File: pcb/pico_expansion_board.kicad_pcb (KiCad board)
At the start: 4 copper layers, 99.1 x 69.8 mm, 53 parts, among them IC1 TPS5450DDA, J1 DC12V/24V, J10 CAN_L, J2 TMC2209 Motor 1, J3 TMC2209 Motor 2, J4 Motor 1, J5 Motor 2, J6 Straight Through, J7 NULL Modem, J8 EXP1, J9 EXP2, SW1 SW_Push, U1 MAX232, U2 MCP2542FDxMF, U3 Pico, U5 CAT24C256

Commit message: Update to v3
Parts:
- removed the C2 at (98.6, 78.5)
- removed the C3 at (94.2, 85.9)
- removed J10: CAN_L, TerminalBlock:TerminalBlock_bornier-2_P5.08mm
- removed J7: NULL Modem, Connector_Dsub:DSUB-9_Male_Horizontal_P2.77x2.84mm_EdgePinOffset7.70mm_Housed_MountingHolesOffset9.12mm
- removed JP9: 120JP, Connector_PinHeader_2.00mm:PinHeader_1x02_P2.00mm_Vertical
- removed the R1 at (111.3, 72.1)
- removed the TP5 at (89.2, 102.9)
- removed the U2 at (94.2, 80.5)
- added C14: 0.1uF, Capacitor_SMD:C_0805_2012Metric_Pad1.18x1.45mm_HandSolder, F.Cu at (94.9, 49.1)
- added C15: 10nF, Capacitor_SMD:C_0805_2012Metric_Pad1.18x1.45mm_HandSolder, F.Cu at (33.0, 106.7)
- added C16: 10nF, Capacitor_SMD:C_0805_2012Metric_Pad1.18x1.45mm_HandSolder, F.Cu at (33.0, 109.7)
- added D2: GREEN, Diode_SMD:D_0805_2012Metric_Pad1.15x1.40mm_HandSolder, F.Cu at (24.0, 106.7)
- added D3: RED, Diode_SMD:D_0805_2012Metric_Pad1.15x1.40mm_HandSolder, F.Cu at (24.0, 109.7)
- added D4: RED, Diode_SMD:D_0805_2012Metric_Pad1.15x1.40mm_HandSolder, F.Cu at (24.0, 112.7)
- added JP5: ~, Connector_PinSocket_2.00mm:PinSocket_1x03_P2.00mm_Vertical, F.Cu at (39.1, 81.9)
- added JP6: ~, Connector_PinSocket_2.00mm:PinSocket_1x03_P2.00mm_Vertical, F.Cu at (43.2, 81.9)
- added JP7: ~, Connector_PinSocket_2.00mm:PinSocket_1x03_P2.00mm_Vertical, F.Cu at (47.2, 81.9)
- added R3: 10K, Resistor_SMD:R_0805_2012Metric_Pad1.20x1.40mm_HandSolder, F.Cu at (88.1, 92.5)
- added R5: 10K, Resistor_SMD:R_0805_2012Metric_Pad1.20x1.40mm_HandSolder, F.Cu at (88.1, 96.8)
- added R6: 4.7k, Resistor_SMD:R_0805_2012Metric_Pad1.20x1.40mm_HandSolder, F.Cu at (94.9, 52.1)
- added R7: 300, Resistor_SMD:R_0805_2012Metric_Pad1.20x1.40mm_HandSolder, F.Cu at (28.6, 106.6)
- added R8: 680, Resistor_SMD:R_0805_2012Metric_Pad1.20x1.40mm_HandSolder, F.Cu at (28.6, 109.6)
- added R9: 4.7k, Resistor_SMD:R_0805_2012Metric_Pad1.20x1.40mm_HandSolder, F.Cu at (28.6, 112.5)
- added U4: 74LVC1G125, Package_TO_SOT_SMD:SOT-353_SC-70-5_Handsoldering, F.Cu at (100.3, 50.5)
- added U5: AMS1117-3.3, Package_TO_SOT_SMD:SOT-223-3_TabPin2, F.Cu at (26.5, 101.0)
- C1: renamed from C5; footprint Capacitor_SMD:C_0805_2012Metric -> Capacitor_SMD:C_0805_2012Metric_Pad1.18x1.45mm_HandSolder
- C10: renamed from C17; footprint Capacitor_SMD:C_0805_2012Metric -> Capacitor_SMD:C_0805_2012Metric_Pad1.18x1.45mm_HandSolder
- C11: renamed from C8; value 10uF -> 0.1uF; footprint Capacitor_SMD:C_0805_2012Metric -> Capacitor_SMD:C_0805_2012Metric_Pad1.18x1.45mm_HandSolder
- C13: renamed from C19; footprint Capacitor_SMD:C_0805_2012Metric -> Capacitor_SMD:C_0805_2012Metric_Pad1.18x1.45mm_HandSolder
- C2: renamed from C1; value 1uF -> 0.1uF; footprint Capacitor_SMD:C_0805_2012Metric -> Capacitor_SMD:C_0805_2012Metric_Pad1.18x1.45mm_HandSolder
- C3: renamed from C9; footprint Capacitor_SMD:C_0805_2012Metric -> Capacitor_SMD:C_0805_2012Metric_Pad1.18x1.45mm_HandSolder
- C4: renamed from C16; footprint Capacitor_SMD:C_0805_2012Metric -> Capacitor_SMD:C_0805_2012Metric_Pad1.18x1.45mm_HandSolder
- C5: renamed from C4; value 1uF -> 0.1uF; footprint Capacitor_SMD:C_0805_2012Metric -> Capacitor_SMD:C_0805_2012Metric_Pad1.18x1.45mm_HandSolder
- C6: value 1uF -> 0.1uF; footprint Capacitor_SMD:C_0805_2012Metric -> Capacitor_SMD:C_0805_2012Metric_Pad1.18x1.45mm_HandSolder
- C7: value 10uF -> 0.1uF; footprint Capacitor_SMD:C_0805_2012Metric -> Capacitor_SMD:C_0805_2012Metric_Pad1.18x1.45mm_HandSolder
- D1: footprint Extra Footprints:DO-214AC -> Diode_SMD:D_SMA
- H1, H2, H3, H4: value MountingHole -> ~
- J6: value Straight Through -> ~
- R1: renamed from R2; footprint Resistor_SMD:R_0805_2012Metric -> Resistor_SMD:R_0805_2012Metric_Pad1.20x1.40mm_HandSolder
- R2: renamed from R6; footprint Resistor_SMD:R_0805_2012Metric -> Resistor_SMD:R_0805_2012Metric_Pad1.20x1.40mm_HandSolder
- R4: renamed from R3; footprint Resistor_SMD:R_0805_2012Metric -> Resistor_SMD:R_0805_2012Metric_Pad1.20x1.40mm_HandSolder
- TP1: renamed from TP6; value TestPoint -> ~
- TP2: renamed from TP7; value TestPoint -> ~
- TP3: renamed from TP8; value TestPoint -> ~
- TP4: renamed from TP1; value TestPoint -> ~
- TP5: renamed from TP2; value TestPoint -> ~
- U1: value MAX232 -> MAX3232
- renumbered C18 to C12, C11 to C8, C12 to C9, TP4 to TP_UART1, U3 to U2, U5 to U3
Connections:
- C11 pad 2: +5V -> GND
- C5 pad 1: +5V -> +3.3V
- J2 pad 15: +5V -> +3.3V
- J2 pad 3: GND -> unconnected-(J2-CLK-Pad3)
- J3 pad 15: +5V -> +3.3V
- J3 pad 3: GND -> unconnected-(J3-CLK-Pad3)
- J3 pad 7: +5V -> +3.3V
- J6 pad 2: SCALE_RXD -> RS232_PIN2
- J6 pad 3: SCALE_TXD -> RS232_PIN3
- J8 pad 6: NEOPIXEL -> NEOPIXEL_5V
- JP1 pad 1: MOTOR_UART -> Net-(J2-PDN)
- JP1 pad 2: Net-(J2-PDN) -> MOTOR_UART
- JP3 pad 1: MOTOR_UART -> Net-(J3-PDN)
- JP3 pad 2: Net-(J3-PDN) -> MOTOR_UART
- U1 pad 16: +5V -> +3.3V
- U2 pad 17: Net-(U3-GPIO13) -> NEOPIXEL
- U2 pad 31: NEOPIXEL -> unconnected-(U2-GPIO26_ADC0-Pad31)
- U2 pad 32: CAN_TX -> unconnected-(U2-GPIO27_ADC1-Pad32)
- U2 pad 34: CAN_RX -> unconnected-(U2-GPIO28_ADC2-Pad34)
- U2 pad 36: +3.3V -> 3.3V_PICO
- U3 pad 8: +5V -> +3.3V
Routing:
- net Net-(J10-Pin_1): track 48.2 -> 0.00 mm
- net Net-(J10-Pin_2): track 39.0 -> 0.00 mm, vias 1 -> 0
- net +5V: track 51.2 -> 36.0 mm, vias 9 -> 5
- net CAN_TX: track 12.2 -> 0.00 mm, vias 1 -> 0
- net CAN_RX: track 11.0 -> 0.00 mm
- net NEOPIXEL: track 40.0 -> 33.5 mm
- net GND: track 85.2 -> 78.8 mm, vias 12 -> 10
- net Net-(U3-GPIO13): track 4.06 -> 0.00 mm
- net Net-(JP9-A): track 3.45 -> 0.00 mm
- net LED_SCK: track 41.0 -> 44.1 mm, vias 0 -> 1
- net 3.3V_PICO: track 0.00 -> 2.57 mm, vias 0 -> 1
- net +3.3V: track 9.86 -> 9.96 mm, vias 0 -> 4
- added copper zone on In2.Cu, net +3.3V
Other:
- board text added: "OpenTricker Controller v0.3"
- board text removed: "120Ω"
- board text removed: "CAN-FD"
- board text removed: "H L"
- board text removed: "OpenTricker Controller v0.2"

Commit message: Update v0.3 PCB
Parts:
- removed JP1: M1_UART_OP1, Connector_PinHeader_2.00mm:PinHeader_1x02_P2.00mm_Vertical
- removed JP2: M1_UART_OP2, Connector_PinHeader_2.00mm:PinHeader_1x02_P2.00mm_Vertical
- removed JP3: M2_UART_OP1, Connector_PinSocket_2.00mm:PinSocket_1x02_P2.00mm_Vertical
- removed JP4: M2_UART_OP2, Connector_PinSocket_2.00mm:PinSocket_1x02_P2.00mm_Vertical
- D1: footprint Diode_SMD:D_SMA -> Extra Footprints:DO-214AC
- J2, J3: footprint fab:Conn_StepStick -> Extra Footprints:Conn_StepStick_smaller_hole
- TP_UART1: value TestPoint -> ~
- U4: footprint Package_TO_SOT_SMD:SOT-353_SC-70-5_Handsoldering -> Package_TO_SOT_SMD:SOT-23-5
- moved U5 131.5 mm to (158.0, 98.3), turned to -90 degrees
- moved H4 130.6 mm to (27.1, 157.6)
- moved D2 129.5 mm to (153.4, 109.9)
- moved D3 129.5 mm to (153.4, 112.9)
- moved D4 129.5 mm to (153.4, 116.0)
- moved R7 129.5 mm to (158.0, 109.8)
- moved R8 129.5 mm to (158.0, 112.8)
- moved R9 129.5 mm to (158.0, 115.7)
- moved C16 126.5 mm to (158.2, 91.9)
- moved C15 125.3 mm to (158.2, 104.6)
- moved JP6 107.9 mm to (150.4, 94.4), turned to 180 degrees
- moved JP5 104.4 mm to (142.7, 94.4), turned to 180 degrees
- moved H3 94.2 mm to (27.1, 149.6)
- moved JP7 88.5 mm to (135.3, 90.4), turned to -90 degrees
- moved H1 76.0 mm to (27.1, 133.7)
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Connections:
- C10 pad 2: Net-(IC1-PH) -> /PH_NET
- IC1 pad 8: Net-(IC1-PH) -> /PH_NET
- J2 pad 4: Net-(J2-PDN) -> unconnected-(J2-PDN-Pad4)
- J2 pad 5: Net-(J2-UART) -> MOTOR_UART
- J3 pad 4: Net-(J3-PDN) -> unconnected-(J3-PDN-Pad4)
- J3 pad 5: Net-(J3-UART) -> MOTOR_UART
- L1 pad 1: Net-(IC1-PH) -> /PH_NET
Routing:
- net 3.3V_REG: track 0.00 -> 46.5 mm
- net SCALE_UART_TX: track 73.7 -> 31.5 mm, vias 1 -> 2
- net GND: track 78.8 -> 45.4 mm, vias 10 -> 19
- net SCALE_UART_RX: track 65.5 -> 33.7 mm, vias 1 -> 2
- net BTN_ENC: track 32.2 -> 60.3 mm, vias 1 -> 0
- net NEOPIXEL: track 33.5 -> 9.92 mm, vias 1 -> 0
- net SCALE_TXD: track 55.7 -> 32.4 mm, vias 0 -> 1
- net RS232_PIN2: track 0.00 -> 22.8 mm
- net Net-(IC1-PH): track 17.6 -> 0.00 mm
- net RS232_PIN3: track 0.00 -> 17.3 mm
- net NEOPIXEL_5V: track 0.00 -> 14.3 mm
- net SCALE_RXD: track 57.0 -> 47.0 mm
- net Net-(J2-PDN): track 9.09 -> 0.00 mm
- net Net-(J3-PDN): track 9.02 -> 0.00 mm
- net PICO_RESET_BTN: track 30.5 -> 22.0 mm, vias 1 -> 2
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- added copper zone on F.Cu, net +5V
- added copper zone on F.Cu, net /PH_NET
- added copper zone on F.Cu, net GND
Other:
- board size 99.1 x 69.8 mm -> 91.7 x 66.8 mm
- board text removed: "DCIN GND"
- board text removed: "EXP1"
- board text removed: "EXP2"
- board text removed: "GND DCIN"
- board text removed: "Motor 1 ADDR 0"
- board text removed: "Motor 2 ADDR 1"
- board text removed: "NULL Modem"
- board text removed: "OpenTricker Controller v0.3"
- board text removed: "PDN/UART"
- board text removed: "RESET"
- board text removed: "Raspberry Pi Pico"
- board text removed: "Straight Through"

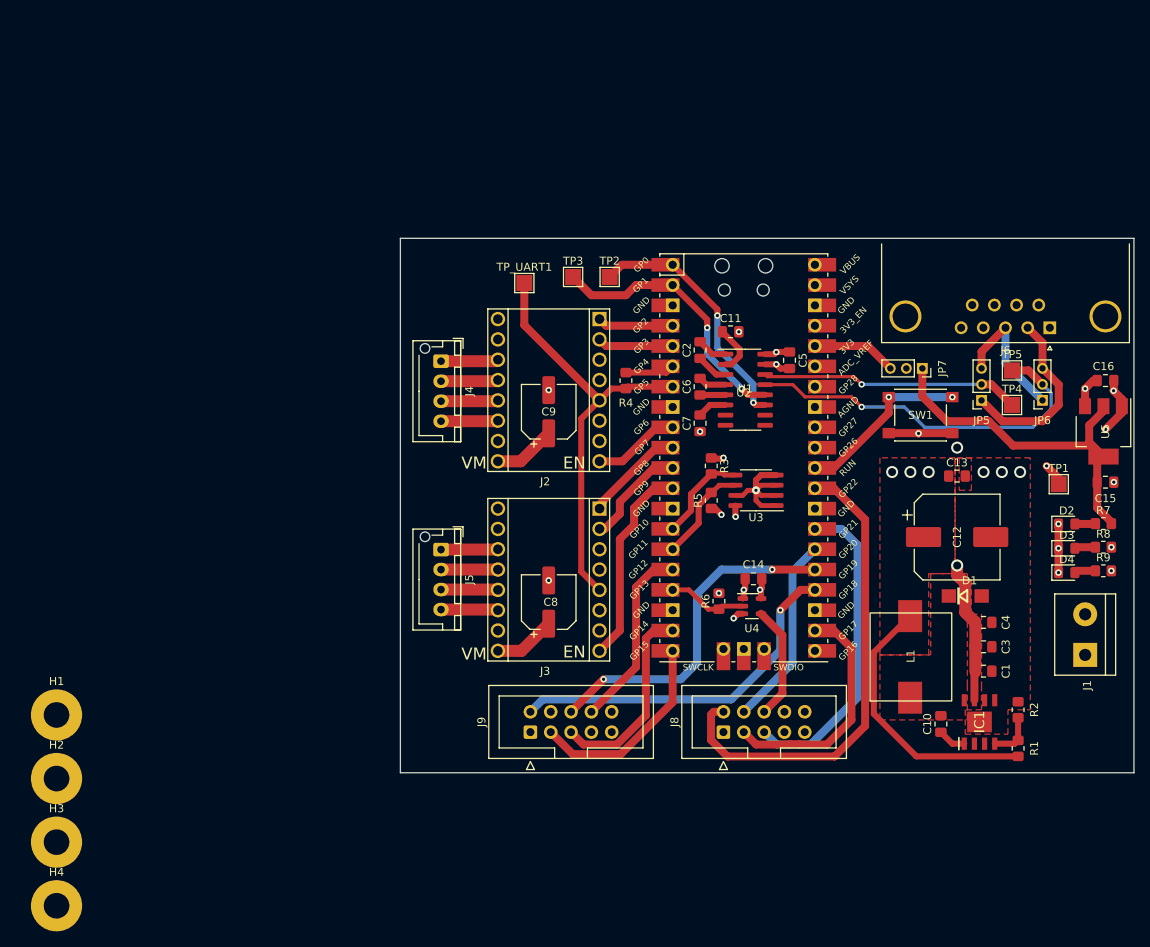
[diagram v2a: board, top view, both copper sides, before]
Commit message: Route v0.3 PCB
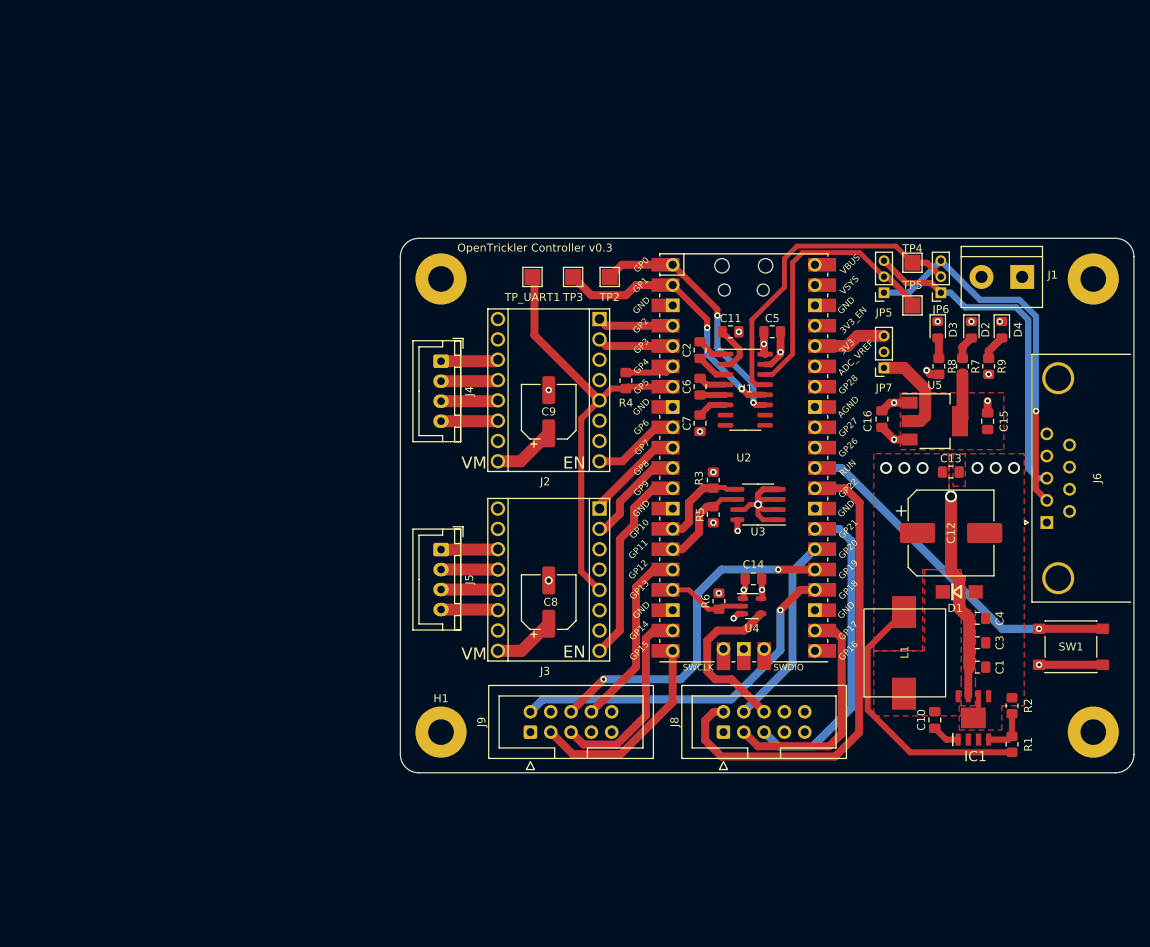
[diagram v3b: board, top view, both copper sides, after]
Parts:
- removed TP1: ~, TestPoint:TestPoint_Pad_2.0x2.0mm
- D3: value RED -> ORANGE
- J4, J5: footprint Connector_JST:JST_XH_B4B-XH-AM_1x04_P2.50mm_Vertical -> Connector_JST:JST_XH_B4B-XH-A_1x04_P2.50mm_Vertical
- moved H3 147.5 mm to (156.7, 79.2)
- moved H4 131.4 mm to (156.7, 135.9)
- moved H2 78.8 mm to (75.2, 79.2)
- moved H1 48.1 mm to (75.2, 135.9)
- moved J1 47.9 mm to (147.8, 79.0), turned to 180 degrees
- moved SW1 34.5 mm to (153.9, 125.2)
- moved D3 31.7 mm to (137.3, 85.6), turned to -90 degrees
- moved D4 31.4 mm to (145.3, 85.6), turned to -90 degrees
- moved R8 30.6 mm to (137.4, 90.2), turned to -90 degrees
- moved R9 29.3 mm to (143.6, 90.2), turned to -90 degrees
- moved C16 28.4 mm to (130.3, 96.8), turned to 90 degrees
- moved D2 27.0 mm to (141.5, 85.6), turned to -90 degrees
- moved R7 26.4 mm to (140.4, 90.2), turned to -90 degrees
- moved J6 24.3 mm to (150.9, 109.7), turned to 90 degrees
- moved U5 21.1 mm to (136.9, 97.0), turned to 0 degrees
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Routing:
- net 3.3V_REG: track 46.5 -> 17.8 mm
- net RS232_PIN3: track 17.3 -> 42.5 mm
- net RS232_PIN2: track 22.8 -> 47.1 mm, vias 0 -> 1
- net PICO_RESET_BTN: track 22.0 -> 44.3 mm, vias 2 -> 1
- net VCC: track 51.0 -> 70.5 mm, vias 4 -> 2
- net NEOPIXEL_5V: track 14.3 -> 21.1 mm
- net SCALE_RXD: track 47.0 -> 40.6 mm, vias 1 -> 0
- net +3.3V: track 7.77 -> 4.27 mm
- net GND: track 45.4 -> 42.3 mm, vias 19 -> 18
- net SCALE_TXD: track 32.4 -> 34.5 mm, vias 1 -> 0
- net +5V: track 41.0 -> 42.7 mm
- net 3.3V_PICO: track 10.6 -> 9.16 mm
- net BTN_ENC: track 60.3 -> 61.6 mm
- net Net-(D4-A): track 2.64 -> 3.23 mm
- net LCD_CS: track 29.9 -> 29.3 mm
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- added copper zone on F.Cu, net 3.3V_REG
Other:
- outline, holes or cut-outs redrawn
- board text added: "EXP1"
- board text added: "EXP2"
- board text added: "NULL"
- board text added: "OpenTrickler Controller v0.3"
- board text added: "Straight"

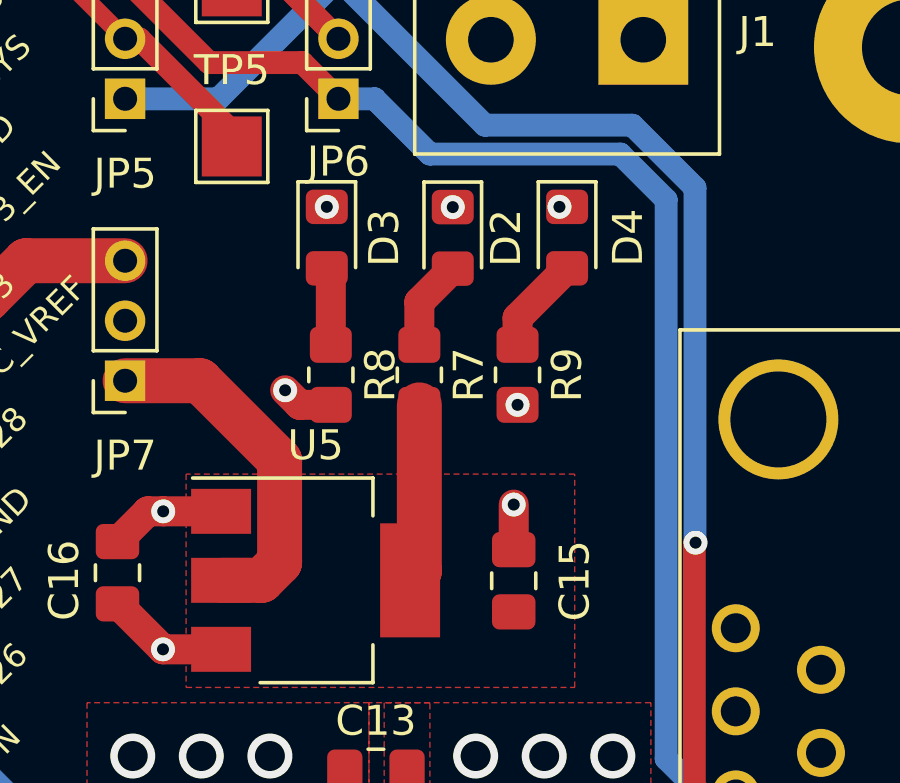
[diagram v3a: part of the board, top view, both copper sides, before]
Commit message: Add LCSC mapping, update BOM, update some placement of components
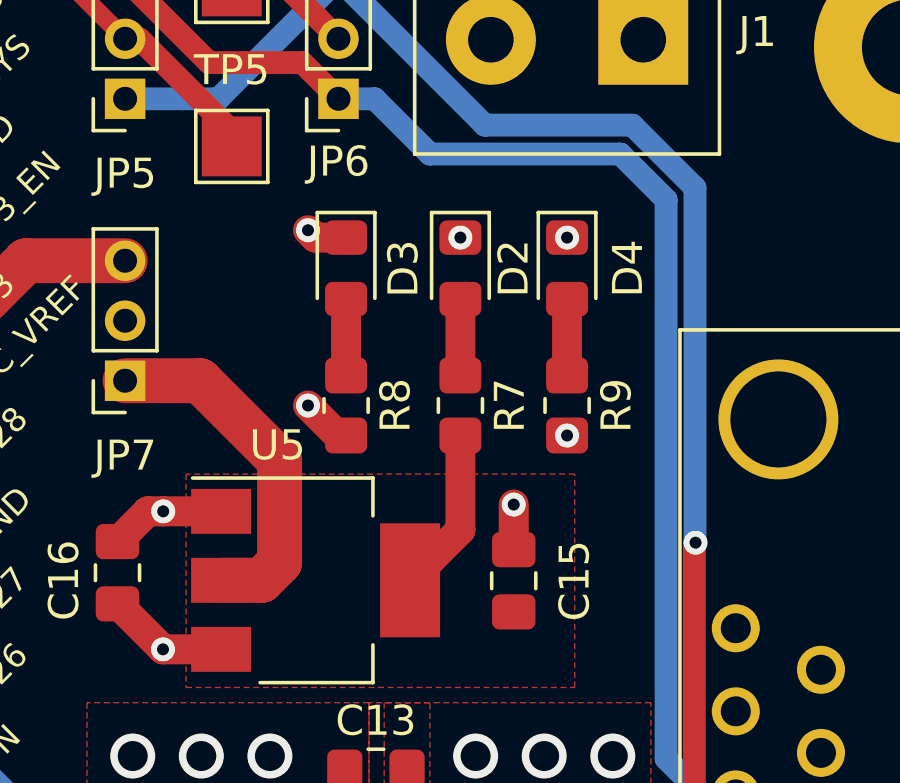
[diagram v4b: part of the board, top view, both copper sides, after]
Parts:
- C11, C14, C2, C5, C6, C7: value 0.1uF -> 100nF
- moved R9 1.94 mm to (145.3, 91.2)
- moved R7 1.71 mm to (141.7, 91.2)
- moved D3 1.21 mm to (137.9, 86.6)
- moved R8 1.14 mm to (137.9, 91.2)
- moved D2 1.05 mm to (141.7, 86.6)
- moved D4 1.03 mm to (145.3, 86.6)
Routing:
- net GND: track 42.3 -> 43.7 mm
- net Net-(D4-A): track 3.23 -> 2.55 mm
